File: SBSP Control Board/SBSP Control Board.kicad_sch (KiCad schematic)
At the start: 42 parts, among them J1 Conn_02x08_Odd_Even, J10 Conn_Coaxial, J11 Conn_Coaxial, J12 Conn_Coaxial, J13 Conn_Coaxial, J14 Conn_Coaxial, J15 Conn_Coaxial, J16 Conn_Coaxial, J17 Conn_Coaxial, J18 Conn_01x02_Socket, J19 Conn_01x02_Socket, J2 Conn_Coaxial, J3 Conn_Coaxial, J4 Conn_Coaxial, J5 Conn_Coaxial, J6 Conn_Coaxial, J7 Conn_Coaxial, J8 Conn_Coaxial, J9 Conn_Coaxial, U1 ADAR1000ACCZN

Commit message: 'finished' the first IC routing
need to re do and see what connections we need to make for programming. also need to see about better ground connections to the IC.
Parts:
- C11, C12, C13, C14, C4, C5, C59, C6, C60, C61, C7: footprint Capacitor_SMD:C_1206_3216Metric -> Resistor_SMD:R_0603_1608Metric
- J1: footprint (none) -> Resistor_SMD:R_0603_1608Metric
- R10, R11, R12, R2, R3, R4, R5, R6, R7, R8, R9: footprint Resistor_SMD:R_1206_3216Metric -> Resistor_SMD:R_0603_1608Metric
- U1: footprint CC-88-1_ADI -> adar1000:CC-88-1_ADI
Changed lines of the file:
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@@
 			)
 		)
-		(property "Footprint" "Resistor_SMD:R_1206_3216Metric"
+		(property "Footprint" "Resistor_SMD:R_0603_1608Metric"
 			(at 22.86 34.798 90)
 			(hide yes)
@@
 			)
 		)
-		(property "Footprint" "Resistor_SMD:R_1206_3216Metric"
+		(property "Footprint" "Resistor_SMD:R_0603_1608Metric"
 			(at 178.308 74.93 90)
 			(hide yes)
@@
 			)
 		)
-		(property "Footprint" "Capacitor_SMD:C_1206_3216Metric"
+		(property "Footprint" "Resistor_SMD:R_0603_1608Metric"
 			(at 23.8252 137.16 0)
 			(hide yes)
@@
 			)
 		)
-		(property "Footprint" ""
+		(property "Footprint" "Resistor_SMD:R_0603_1608Metric"
 			(at 196.85 33.02 0)
 			(hide yes)
@@
 		(exclude_from_sim no)
 		(in_bom yes)
-		(on_board yes)
+		(on_board no)
 		(in_pos_files yes)
 		(dnp no)
@@
 			)
 		)
-		(property "Footprint" "Capacitor_SMD:C_1206_3216Metric"
+		(property "Footprint" "Resistor_SMD:R_0603_1608Metric"
 			(at 105.1052 167.64 0)
 			(hide yes)
@@
 			)
 		)
-		(property "Footprint" "Resistor_SMD:R_1206_3216Metric"
+		(property "Footprint" "Resistor_SMD:R_0603_1608Metric"
 			(at 166.878 57.15 90)
 			(hide yes)
@@
 			)
 		)
-		(property "Footprint" "CC-88-1_ADI"
+		(property "Footprint" "adar1000:CC-88-1_ADI"
 			(at 40.64 33.02 0)
 			(hide yes)
@@
 		(exclude_from_sim no)
 		(in_bom yes)
-		(on_board yes)
+		(on_board no)
 		(in_pos_files yes)
 		(dnp no)
@@
 			)
 		)
-		(property "Footprint" "Capacitor_SMD:C_1206_3216Metric"
+		(property "Footprint" "Resistor_SMD:R_0603_1608Metric"
 			(at 79.7052 167.64 0)
 			(hide yes)
@@
 			)
 		)
-		(property "Footprint" "Capacitor_SMD:C_1206_3216Metric"
+		(property "Footprint" "Resistor_SMD:R_0603_1608Metric"
 			(at 40.3352 167.64 0)
 			(hide yes)
@@
 			)
 		)
-		(property "Footprint" "Resistor_SMD:R_1206_3216Metric"
+		(property "Footprint" "Resistor_SMD:R_0603_1608Metric"
 			(at 174.498 83.82 90)
 			(hide yes)
@@
 			)
 		)
-		(property "Footprint" "CC-88-1_ADI"
+		(property "Footprint" "adar1000:CC-88-1_ADI"
 			(at 64.77 124.46 0)
 			(hide yes)
@@
 			)
 		)
-		(property "Footprint" "Capacitor_SMD:C_1206_3216Metric"
+		(property "Footprint" "Resistor_SMD:R_0603_1608Metric"
 			(at 46.6852 137.16 0)
 			(hide yes)
@@
 			)
 		)
-		(property "Footprint" "Resistor_SMD:R_1206_3216Metric"
+		(property "Footprint" "Resistor_SMD:R_0603_1608Metric"
 			(at 31.75 37.338 90)
 			(hide yes)
@@
 			)
 		)
-		(property "Footprint" "Resistor_SMD:R_1206_3216Metric"
+		(property "Footprint" "Resistor_SMD:R_0603_1608Metric"
 			(at 149.86 44.958 90)
 			(hide yes)
@@
 			)
 		)
-		(property "Footprint" "Resistor_SMD:R_1206_3216Metric"
+		(property "Footprint" "Resistor_SMD:R_0603_1608Metric"
 			(at 182.118 66.04 90)
 			(hide yes)
@@
 			)
 		)
-		(property "Footprint" "Capacitor_SMD:C_1206_3216Metric"
+		(property "Footprint" "Resistor_SMD:R_0603_1608Metric"
 			(at 119.0752 167.64 0)
 			(hide yes)
@@
 			)
 		)
-		(property "Footprint" "CC-88-1_ADI"
+		(property "Footprint" "adar1000:CC-88-1_ADI"
 			(at 25.4 212.09 0)
 			(hide yes)
@@
 			)
 		)
-		(property "Footprint" "Resistor_SMD:R_1206_3216Metric"
+		(property "Footprint" "Resistor_SMD:R_0603_1608Metric"
 			(at 26.67 65.278 90)
 			(hide yes)
@@
 			)
 		)
-		(property "Footprint" "Resistor_SMD:R_1206_3216Metric"
+		(property "Footprint" "Resistor_SMD:R_0603_1608Metric"
 			(at 170.688 48.26 90)
 			(hide yes)
@@
 			)
 		)
-		(property "Footprint" "Resistor_SMD:R_1206_3216Metric"
+		(property "Footprint" "Resistor_SMD:R_0603_1608Metric"
 			(at 185.928 57.15 90)
 			(hide yes)
@@
 			)
 		)
-		(property "Footprint" "Capacitor_SMD:C_1206_3216Metric"
+		(property "Footprint" "Resistor_SMD:R_0603_1608Metric"
 			(at 67.0052 167.64 0)
 			(hide yes)
@@
 			)
 		)
-		(property "Footprint" "Resistor_SMD:R_1206_3216Metric"
+		(property "Footprint" "Resistor_SMD:R_0603_1608Metric"
 			(at 192.278 48.26 90)
 			(hide yes)
@@
 			)
 		)
-		(property "Footprint" "Capacitor_SMD:C_1206_3216Metric"
+		(property "Footprint" "Resistor_SMD:R_0603_1608Metric"
 			(at 92.4052 167.64 0)
 			(hide yes)
@@
 		(exclude_from_sim no)
 		(in_bom yes)
-		(on_board yes)
+		(on_board no)
 		(in_pos_files yes)
 		(dnp no)
@@
 			)
 		)
-		(property "Footprint" "Capacitor_SMD:C_1206_3216Metric"
+		(property "Footprint" "Resistor_SMD:R_0603_1608Metric"
 			(at 131.7752 167.64 0)
 			(hide yes)
@@
 		(exclude_from_sim no)
 		(in_bom yes)
-		(on_board yes)
+		(on_board no)
 		(in_pos_files yes)
 		(dnp no)
@@
 			)
 		)
-		(property "Footprint" "Capacitor_SMD:C_1206_3216Metric"
+		(property "Footprint" "Resistor_SMD:R_0603_1608Metric"
 			(at 53.0352 167.64 0)
 			(hide yes)
@@
 			)
 		)
-		(property "Footprint" "Capacitor_SMD:C_1206_3216Metric"
+		(property "Footprint" "Resistor_SMD:R_0603_1608Metric"
 			(at 35.2552 137.16 0)
 			(hide yes)

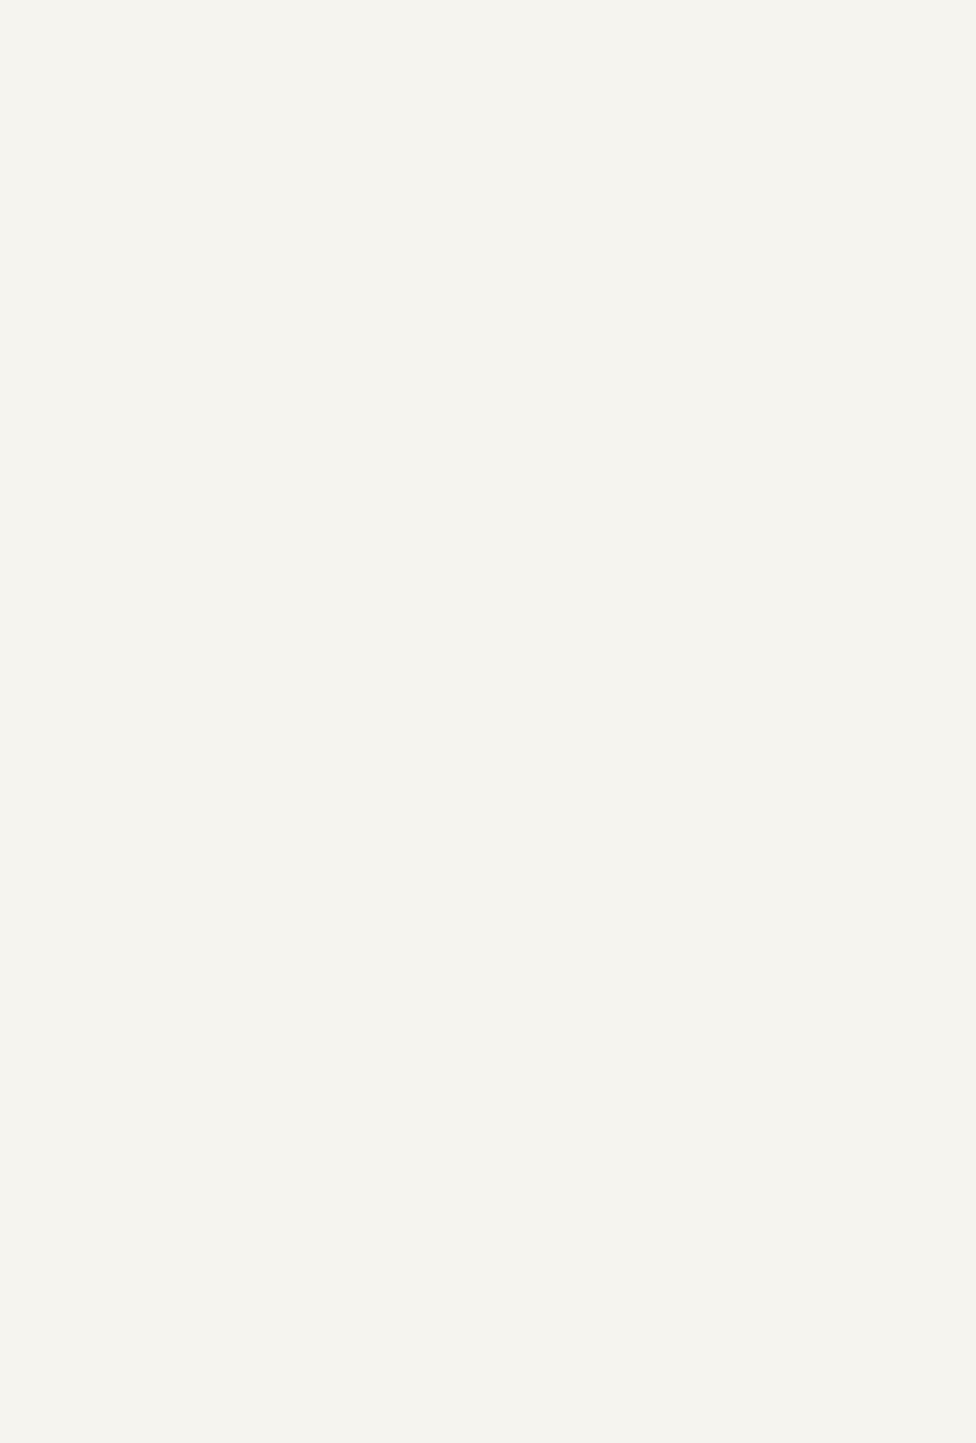
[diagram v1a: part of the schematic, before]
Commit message: finished passive layout for IC's
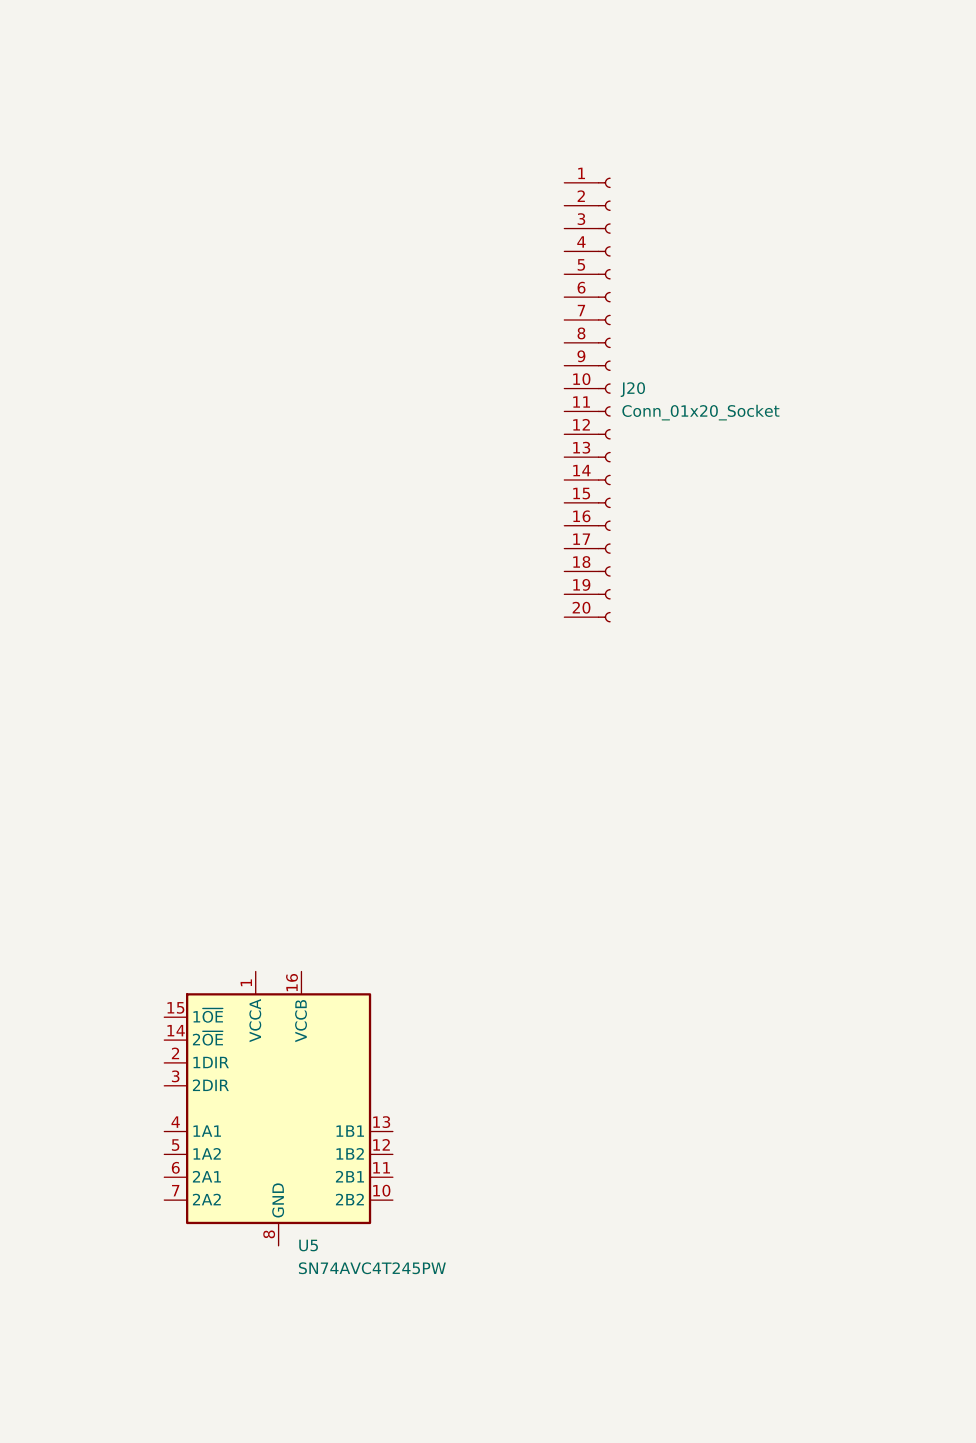
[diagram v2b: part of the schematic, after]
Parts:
- added J20: Conn_01x20_Socket, symbol Connector:Conn_01x20_Socket
- added U5: SN74AVC4T245PW, Package_SO:TSSOP-16_4.4x5mm_P0.65mm, symbol Logic_LevelTranslator:SN74AVC4T245PW
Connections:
- new net: U5.8 (GND), U5.9 (GND)
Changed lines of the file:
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@@
+	)
+	(symbol
+		(lib_id "Connector:Conn_01x20_Socket")
+		(at 299.72 139.7 0)
+		(unit 1)
+		(body_style 1)
+		(exclude_from_sim no)
+		(in_bom yes)
+		(on_board yes)
+		(in_pos_files yes)
+		(dnp no)
+		(fields_autoplaced yes)
+		(property "Reference" "J20"
+			(at 300.99 139.6999 0)
+			(show_name no)
+			(do_not_autoplace no)
+			(effects
+				(font
+					(size 1.27 1.27)
+				)
+				(justify left)
+			)
+		)
+		(property "Value" "Conn_01x20_Socket"
+			(at 300.99 142.2399 0)
+			(show_name no)
+			(do_not_autoplace no)
+			(effects
+				(font
+					(size 1.27 1.27)
+				)
+				(justify left)
+			)
+		)
+		(property "Footprint" ""
+			(at 299.72 139.7 0)
+			(hide yes)
+			(show_name no)
+			(do_not_autoplace no)
+			(effects
+				(font
+					(size 1.27 1.27)
+				)
+			)
+		)
+		(property "Datasheet" ""
+			(at 299.72 139.7 0)
+			(hide yes)
+			(show_name no)
+			(do_not_autoplace no)
+			(effects
+				(font
+					(size 1.27 1.27)
+				)
+			)
+		)
+		(property "Description" "Generic connector, single row, 01x20, script generated"
+			(at 299.72 139.7 0)
+			(hide yes)
+			(show_name no)
+			(do_not_autoplace no)
+			(effects
+				(font
+					(size 1.27 1.27)
+				)
+			)
+		)
+		(pin "6"
+		)
+		(pin "11"
+		)
+		(pin "4"
+		)
+		(pin "7"
+		)
+		(pin "12"
+		)
+		(pin "13"
+		)
+		(pin "3"
+		)
+		(pin "2"
+		)
+		(pin "9"
+		)
+		(pin "10"
+		)
+		(pin "5"
+		)
+		(pin "8"
+		)
+		(pin "14"
+		)
+		(pin "1"
+		)
+		(pin "15"
+		)
+		(pin "16"
+		)
+		(pin "17"
+		)
+		(pin "18"
+		)
+		(pin "19"
+		)
+		(pin "20"
+		)
+		(instances
+			(project "SBSP Control Board"
+				(path "/f73a4dfd-d850-4db8-8b86-55d3699fcce2"
+					(reference "J20")
+					(unit 1)
+				)
+			)
+		)
 	)
 	(symbol
@@
 					(unit 1)
 				)
+			)
+		)
+	)
+	(symbol
+		(lib_id "Logic_LevelTranslator:SN74AVC4T245PW")
+		(at 262.89 219.71 0)
+		(unit 1)
+		(body_style 1)
+		(exclude_from_sim no)
+		(in_bom yes)
+		(on_board yes)
+		(in_pos_files yes)
+		(dnp no)
+		(fields_autoplaced yes)
+		(property "Reference" "U5"
+			(at 265.0333 234.95 0)
+			(show_name no)
+			(do_not_autoplace no)
+			(effects
+				(font
+					(size 1.27 1.27)
+				)
+				(justify left)
+			)
+		)
+		(property "Value" "SN74AVC4T245PW"
+			(at 265.0333 237.49 0)
+			(show_name no)
+			(do_not_autoplace no)
+			(effects
+				(font
+					(size 1.27 1.27)
+				)
+				(justify left)
+			)
+		)
+		(property "Footprint" "Package_SO:TSSOP-16_4.4x5mm_P0.65mm"
+			(at 262.89 222.25 0)
+			(hide yes)
+			(show_name no)
+			(do_not_autoplace no)
+			(effects
+				(font
+					(size 1.27 1.27)
+				)
+			)
+		)
+		(property "Datasheet" "https://www.ti.com/lit/ds/symlink/sn74avc4t245.pdf"
+			(at 261.62 226.06 0)
+			(hide yes)
+			(show_name no)
+			(do_not_autoplace no)
+			(effects
+				(font
+					(size 1.27 1.27)
+				)
+			)
+		)
+		(property "Description" "4-Bit Dual-Supply Bus Transceiver With Configurable Voltage Translation and 3-State Outputs, TSSOP-16"
+			(at 262.89 219.71 0)
+			(hide yes)
+			(show_name no)
+			(do_not_autoplace no)
+			(effects
+				(font
+					(size 1.27 1.27)
+				)
+			)
+		)
+		(pin "10"
+		)
+		(pin "7"
+		)
+		(pin "6"
+		)
+		(pin "1"
+		)
+		(pin "16"
+		)
+		(pin "12"
+		)
+		(pin "15"
+		)
+		(pin "14"
+		)
+		(pin "8"
+		)
+		(pin "5"
+		)
+		(pin "4"
+		)
+		(pin "2"
+		)
+		(pin "3"
+		)
+		(pin "13"
+		)
+		(pin "11"
+		)
+		(pin "9"
+		)
+		(instances
+			(project "SBSP Control Board"
+				(path "/f73a4dfd-d850-4db8-8b86-55d3699fcce2"
+					(reference "U5")
+					(unit 1)
+				)

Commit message: added first level shifting circuit
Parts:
- removed J1: Conn_02x08_Odd_Even, Resistor_SMD:R_0603_1608Metric, symbol Connector_Generic:Conn_02x08_Odd_Even
- removed R2: 0, Resistor_SMD:R_0603_1608Metric, symbol Device:R
- removed R3, R4, R5, R6, R7, R8, R9: 22.1k, Resistor_SMD:R_0603_1608Metric, symbol Device:R
- added C62, C64: 0.1uF, Resistor_SMD:R_0603_1608Metric, symbol Device:C
- added C63, C65: 10pF, Resistor_SMD:R_0603_1608Metric, symbol Device:C
- added J21: Conn_01x20_Socket, symbol Connector:Conn_01x20_Socket
- added R16, R19, R20, R22, R25: 0, Resistor_SMD:R_0603_1608Metric, symbol Device:R
- added R17, R18, R21, R23, R24: 10k, Resistor_SMD:R_0603_1608Metric, symbol Device:R
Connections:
- net ADAR_CS_STAGE1_1V8 is gone; now on net CSB: U1.M3 (CSB)
- net ADAR_SCLK_1V8 is gone; now on net SCLK: U1.M6 (SCLK)
- net +1.8V: now also U5.16 (VCCB), C64.2, C65.2
- net AVDD2: now also J20.7 (Pin_7), J21.7 (Pin_7)
- net CSB: now also U5.11 (2B1)
- net GND: now also J20.1 (Pin_1), J20.2 (Pin_2), J20.20 (Pin_20), J20.6 (Pin_6), J20.8 (Pin_8), U5.8 (GND), U5.9 (GND), C62.1, C63.1, C64.1, C65.1, J21.1 (Pin_1), J21.2 (Pin_2), J21.20 (Pin_20), J21.6 (Pin_6), J21.8 (Pin_8), R17.1, R18.1, R23.1, R24.2
- net SCLK: now also U5.13 (1B1)
- net SDO: now also R25.2
- net GPIO1: now reaches J20.10 (Pin_10)
- net GPIO1: now also J21.10 (Pin_10)
- net GPIO2: now reaches J20.11 (Pin_11)
- net GPIO2: now also J21.11 (Pin_11), R19.1
- net GPIO3: now reaches J20.12 (Pin_12)
- net GPIO3: now also J21.12 (Pin_12), R22.1
- net GPIO4: now reaches J20.13 (Pin_13)
- net GPIO4: now also J21.13 (Pin_13)
- net GPIO5: now reaches J20.14 (Pin_14)
- net GPIO5: now also J21.14 (Pin_14)
- net at J20.15 (Pin_15): now also J21.15 (Pin_15), R25.1
- net SPI_CLK: now reaches J20.16 (Pin_16)
- net SPI_CLK: now also J21.16 (Pin_16), R16.1, R17.2
- net SPI_MOSI: now reaches J20.17 (Pin_17)
- net SPI_MOSI: now also J20.19 (Pin_19), J21.17 (Pin_17), R18.2
- net SPI_SEL_A: now reaches J20.18 (Pin_18)
- net SPI_SEL_A: now also J21.18 (Pin_18), R20.1, R21.1
- net AVDD: now reaches J20.3 (Pin_3)
- net AVDD: now also J20.4 (Pin_4), J20.5 (Pin_5), U5.2 (1DIR), U5.3 (2DIR), J21.3 (Pin_3), J21.4 (Pin_4), J21.5 (Pin_5), R23.2
- net GPIO0: now reaches J20.9 (Pin_9)
- net GPIO0: now also J21.9 (Pin_9)
- net +3V3: now reaches U5.1 (VCCA)
- net +3V3: now also C62.2, C63.2, R21.2
- net AD1: now reaches U5.10 (2B2)
- net AD0: now reaches U5.12 (1B2)
- net at U5.14 (2~{OE}): now also U5.15 (1~{OE}), R24.1
- net at U5.4 (1A1): now also R16.2
- net at U5.5 (1A2): now also R19.2
- net at U5.6 (2A1): now also R20.2
- net at U5.7 (2A2): now also R22.2
- new net SPI_MISO: J21.19 (Pin_19)
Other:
- note added: "<----- DVDD is 1.8V"
- note added: "AVDD is just 3v3"
- note removed: "all pull downs DNP - place on back"
- moved on the sheet: J20, U5
